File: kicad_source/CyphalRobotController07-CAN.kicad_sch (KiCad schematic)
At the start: 20 parts, among them J1 BM04B-SRSS-TB, J15 PinHeader_1x04, J16 PinHeader_1x04, J17 PinHeader_1x05, J2 RASPBERRYPI_PICO, J3 BM04B-SRSS-TB, J4 B3B-PH-SM4-TB, SW1 PTS636 SM43 SMTR LFS, U1 24LC64-I/SN

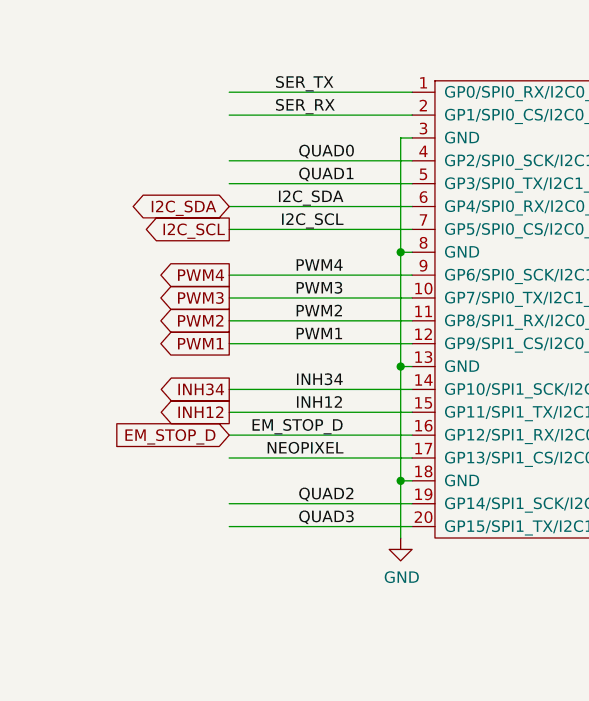
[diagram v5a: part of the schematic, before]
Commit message: added JST XH connector for motor and encoder
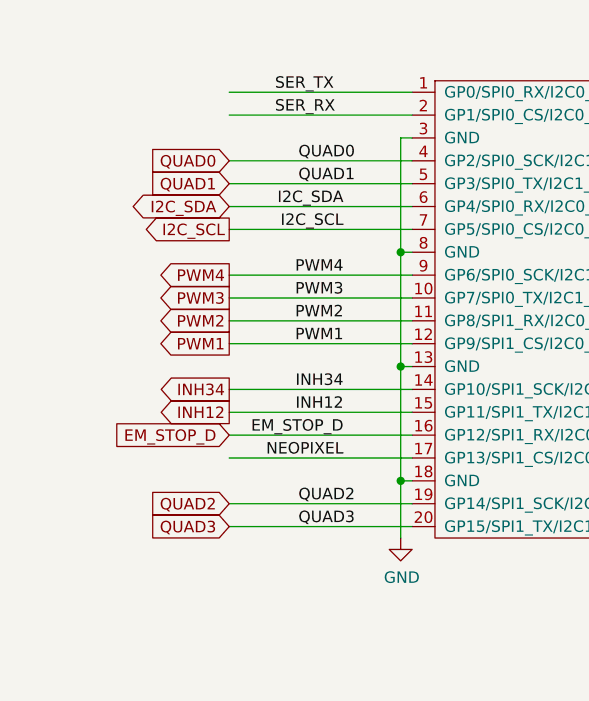
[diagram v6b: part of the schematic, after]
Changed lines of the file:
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@@
+    )
+  )
+  (global_label "QUAD1" (shape input) (at 40.64 41.91 180) (fields_autoplaced)
+    (effects (font (size 1.27 1.27)) (justify right))
+    (property "Referenzen zwischen Schaltplänen" "${INTERSHEET_REFS}" (id 0) (at 32.0868 41.8306 0)
+      (effects (font (size 1.27 1.27)) (justify right) hide)
     )
   )
@@
     )
   )
+  (global_label "QUAD2" (shape input) (at 40.64 77.47 180) (fields_autoplaced)
+    (effects (font (size 1.27 1.27)) (justify right))
+    (property "Referenzen zwischen Schaltplänen" "${INTERSHEET_REFS}" (id 0) (at 32.0868 77.3906 0)
+      (effects (font (size 1.27 1.27)) (justify right) hide)
+    )
+  )
   (global_label "PWM3" (shape output) (at 40.64 54.61 180) (fields_autoplaced)
     (effects (font (size 1.27 1.27)) (justify right))
@@
     )
   )
+  (global_label "QUAD3" (shape input) (at 40.64 80.01 180) (fields_autoplaced)
+    (effects (font (size 1.27 1.27)) (justify right))
+    (property "Referenzen zwischen Schaltplänen" "${INTERSHEET_REFS}" (id 0) (at 32.0868 79.9306 0)
+      (effects (font (size 1.27 1.27)) (justify right) hide)
+    )
+  )
   (global_label "OUTPUT0" (shape output) (at 161.29 64.77 0) (fields_autoplaced)
     (effects (font (size 1.27 1.27)) (justify left))
@@
     (property "Referenzen zwischen Schaltplänen" "${INTERSHEET_REFS}" (id 0) (at -72.39 -7.62 0)
       (effects (font (size 1.27 1.27)) hide)
+    )
+  )
+  (global_label "QUAD0" (shape input) (at 40.64 39.37 180) (fields_autoplaced)
+    (effects (font (size 1.27 1.27)) (justify right))
+    (property "Referenzen zwischen Schaltplänen" "${INTERSHEET_REFS}" (id 0) (at 32.0868 39.2906 0)
+      (effects (font (size 1.27 1.27)) (justify right) hide)
     )
   )
@@
       (reference "#PWR043") (unit 1) (value "GND") (footprint "")
     )
+    (path "/29c3546c-5738-4410-83a1-968e85712add/5bfbf133-5ed7-46d0-b93e-5a5eeb84dcff"
+      (reference "#PWR044") (unit 1) (value "+3.3V") (footprint "")
+    )
+    (path "/29c3546c-5738-4410-83a1-968e85712add/09e143e1-e556-491f-aa8e-93db6198adbc"
+      (reference "#PWR045") (unit 1) (value "GND") (footprint "")
+    )
     (path "/29c3546c-5738-4410-83a1-968e85712add/00000000-0000-0000-0000-00005df76577"
       (reference "#PWR046") (unit 1) (value "GND") (footprint "")
@@
       (reference "#PWR047") (unit 1) (value "GND") (footprint "")
     )
+    (path "/29c3546c-5738-4410-83a1-968e85712add/900bbe2d-04d2-4af8-9360-ab393613f74d"
+      (reference "#PWR048") (unit 1) (value "+3.3V") (footprint "")
+    )
     (path "/29c3546c-5738-4410-83a1-968e85712add/00000000-0000-0000-0000-00005df4db84"
       (reference "#PWR049") (unit 1) (value "GND") (footprint "")
@@
       (reference "#PWR069") (unit 1) (value "GND") (footprint "")
     )
+    (path "/29c3546c-5738-4410-83a1-968e85712add/99d4c74d-1d3b-4c55-ad7e-4e7a828dae09"
+      (reference "#PWR070") (unit 1) (value "GND") (footprint "")
+    )
     (path "/f22e738d-7eb9-478a-98ea-a8bc262180f6/00000000-0000-0000-0000-00005de82a78"
       (reference "#PWR071") (unit 1) (value "GND") (footprint "")
@@
       (reference "J18") (unit 1) (value "Conn_01x02") (footprint "Connector_Phoenix_MC:PhoenixContact_MC_1,5_2-G-3.81_1x02_P3.81mm_Horizontal")
     )
+    (path "/29c3546c-5738-4410-83a1-968e85712add/c27c1f18-6b03-4d6c-bd65-28137af7a5e4"
+      (reference "J19") (unit 1) (value "S6B-XH-A") (footprint "Connector_JST:JST_XH_S6B-XH-A_1x06_P2.50mm_Horizontal")
+    )
+    (path "/29c3546c-5738-4410-83a1-968e85712add/9ba7b6bd-56ab-4aef-8340-78cdea895920"
+      (reference "J20") (unit 1) (value "S6B-XH-A") (footprint "Connector_JST:JST_XH_S6B-XH-A_1x06_P2.50mm_Horizontal")
+    )
     (path "/00000000-0000-0000-0000-0000625bb6fe"

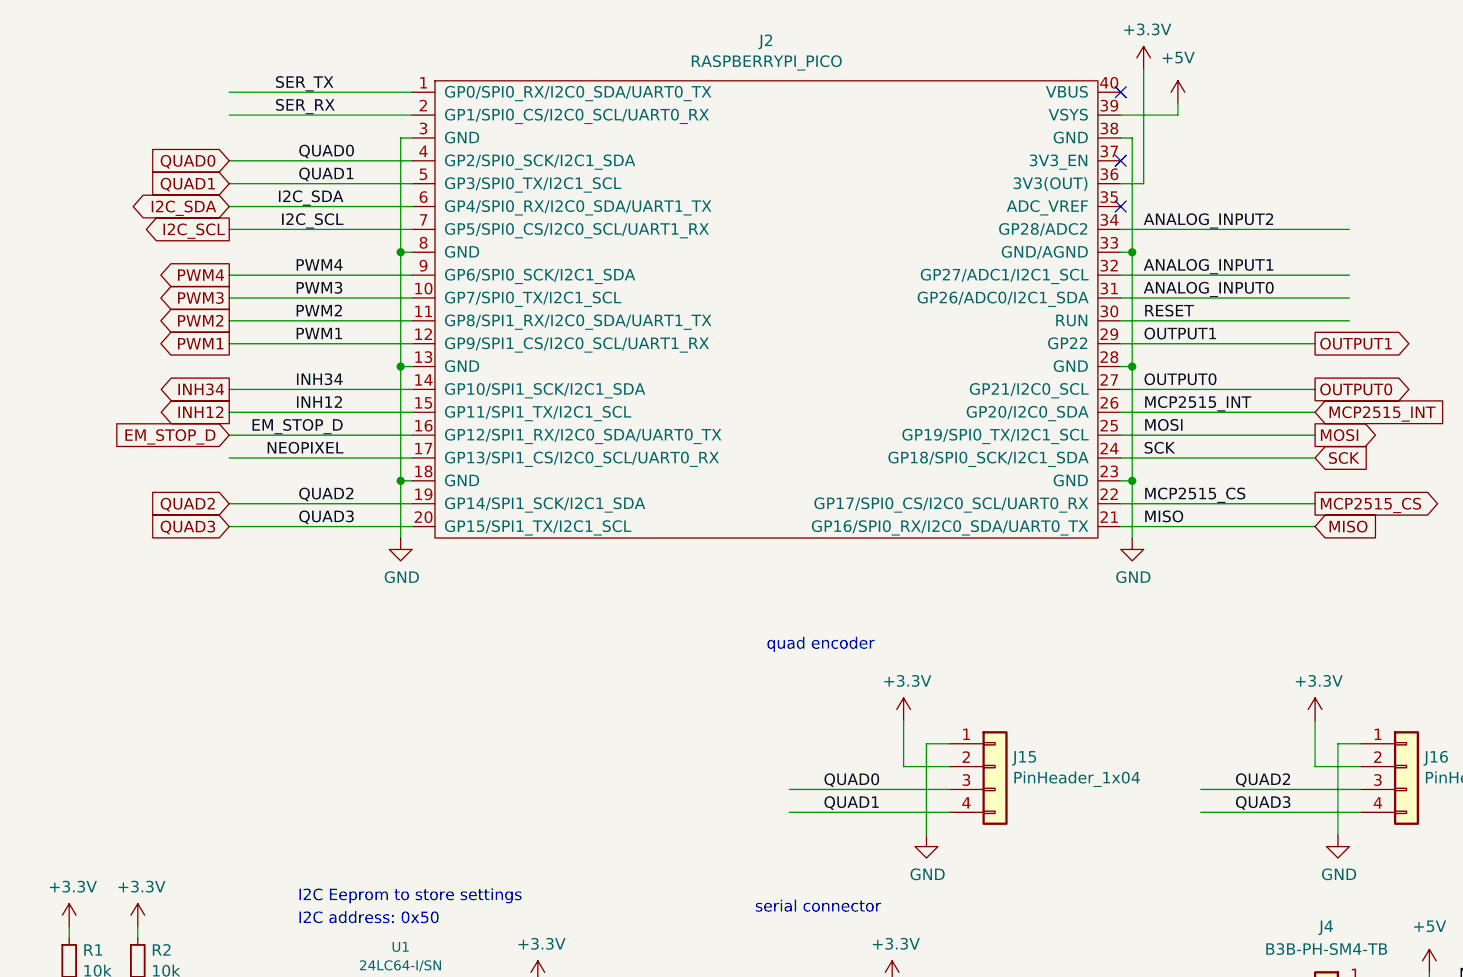
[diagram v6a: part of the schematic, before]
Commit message: changed motor connector, connected encoder
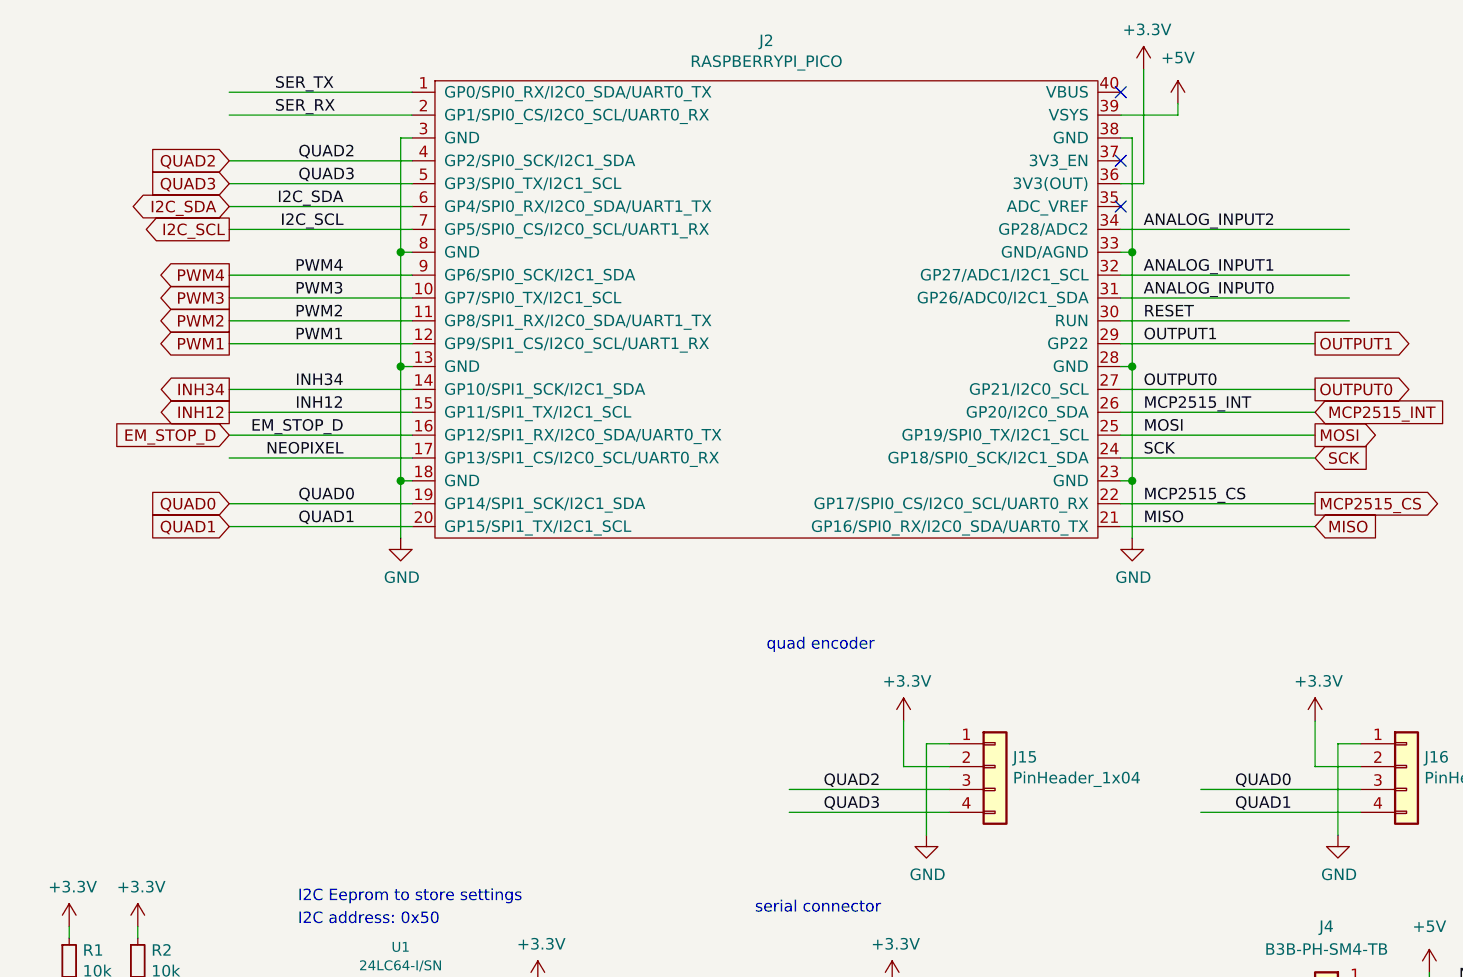
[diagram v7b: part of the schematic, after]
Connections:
- net QUAD0: now also J16.3 (Pin_3), J2.19 (GP14/SPI1_SCK/I2C1_SDA); no longer J15.3 (Pin_3), J2.4 (GP2/SPI0_SCK/I2C1_SDA)
- net QUAD1: now also J16.4 (Pin_4), J2.20 (GP15/SPI1_TX/I2C1_SCL); no longer J15.4 (Pin_4), J2.5 (GP3/SPI0_TX/I2C1_SCL)
- net QUAD2: now also J15.3 (Pin_3), J2.4 (GP2/SPI0_SCK/I2C1_SDA); no longer J16.3 (Pin_3), J2.19 (GP14/SPI1_SCK/I2C1_SDA)
- net QUAD3: now also J15.4 (Pin_4), J2.5 (GP3/SPI0_TX/I2C1_SCL); no longer J16.4 (Pin_4), J2.20 (GP15/SPI1_TX/I2C1_SCL)
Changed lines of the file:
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@@
   (title_block
     (title "CyphalRobotController07/CAN")
-    (date "2023-12-03")
+    (date "2024-01-04")
     (rev "0.2")
     (company "generationmake")
@@
     (effects (font (size 1.27 1.27)) (justify left bottom))
   )
-  (label "QUAD1" (at 106.68 111.76 0)
+  (label "QUAD3" (at 106.68 111.76 0)
     (effects (font (size 1.27 1.27)) (justify left bottom))
   )
@@
     (effects (font (size 1.27 1.27)) (justify left bottom))
   )
-  (label "QUAD0" (at 106.68 109.22 0)
+  (label "QUAD2" (at 106.68 109.22 0)
     (effects (font (size 1.27 1.27)) (justify left bottom))
   )
@@
     (effects (font (size 1.27 1.27)) (justify right bottom))
   )
-  (label "QUAD2" (at 152.4 109.22 0)
-    (effects (font (size 1.27 1.27)) (justify left bottom))
-  )
-  (label "QUAD1" (at 54.61 41.91 180)
+  (label "QUAD0" (at 152.4 109.22 0)
+    (effects (font (size 1.27 1.27)) (justify left bottom))
+  )
+  (label "QUAD3" (at 54.61 41.91 180)
     (effects (font (size 1.27 1.27)) (justify right bottom))
   )
@@
     (effects (font (size 1.27 1.27)) (justify right bottom))
   )
-  (label "QUAD3" (at 152.4 111.76 0)
+  (label "QUAD1" (at 152.4 111.76 0)
     (effects (font (size 1.27 1.27)) (justify left bottom))
   )
@@
     (effects (font (size 1.27 1.27)) (justify right bottom))
   )
-  (label "QUAD2" (at 54.61 77.47 180)
+  (label "QUAD0" (at 54.61 77.47 180)
     (effects (font (size 1.27 1.27)) (justify right bottom))
   )
@@
     (effects (font (size 1.27 1.27)) (justify left bottom))
   )
-  (label "QUAD0" (at 54.61 39.37 180)
+  (label "QUAD2" (at 54.61 39.37 180)
     (effects (font (size 1.27 1.27)) (justify right bottom))
   )
@@
     (effects (font (size 1.27 1.27)) (justify left bottom))
   )
-  (label "QUAD3" (at 54.61 80.01 180)
+  (label "QUAD1" (at 54.61 80.01 180)
     (effects (font (size 1.27 1.27)) (justify right bottom))
   )
@@
     )
   )
-  (global_label "QUAD1" (shape input) (at 40.64 41.91 180) (fields_autoplaced)
+  (global_label "QUAD3" (shape input) (at 40.64 41.91 180) (fields_autoplaced)
     (effects (font (size 1.27 1.27)) (justify right))
     (property "Referenzen zwischen Schaltplänen" "${INTERSHEET_REFS}" (id 0) (at 32.0868 41.8306 0)
@@
     )
   )
-  (global_label "QUAD2" (shape input) (at 40.64 77.47 180) (fields_autoplaced)
+  (global_label "QUAD0" (shape input) (at 40.64 77.47 180) (fields_autoplaced)
     (effects (font (size 1.27 1.27)) (justify right))
     (property "Referenzen zwischen Schaltplänen" "${INTERSHEET_REFS}" (id 0) (at 32.0868 77.3906 0)
@@
     )
   )
-  (global_label "QUAD3" (shape input) (at 40.64 80.01 180) (fields_autoplaced)
+  (global_label "QUAD1" (shape input) (at 40.64 80.01 180) (fields_autoplaced)
     (effects (font (size 1.27 1.27)) (justify right))
     (property "Referenzen zwischen Schaltplänen" "${INTERSHEET_REFS}" (id 0) (at 32.0868 79.9306 0)
@@
     )
   )
-  (global_label "QUAD0" (shape input) (at 40.64 39.37 180) (fields_autoplaced)
+  (global_label "QUAD2" (shape input) (at 40.64 39.37 180) (fields_autoplaced)
     (effects (font (size 1.27 1.27)) (justify right))
     (property "Referenzen zwischen Schaltplänen" "${INTERSHEET_REFS}" (id 0) (at 32.0868 39.2906 0)
@@
     )
     (path "/29c3546c-5738-4410-83a1-968e85712add/00000000-0000-0000-0000-00005ddbb53a"
-      (reference "J8") (unit 1) (value "x") (footprint "Connector_Phoenix_MC:PhoenixContact_MC_1,5_2-G-3.81_1x02_P3.81mm_Horizontal")
+      (reference "J8") (unit 1) (value "x") (footprint "Connector_Phoenix_MSTB:PhoenixContact_MSTBA_2,5_2-G-5,08_1x02_P5.08mm_Horizontal")
     )
     (path "/29c3546c-5738-4410-83a1-968e85712add/00000000-0000-0000-0000-00005ddbbd18"
-      (reference "J9") (unit 1) (value "x") (footprint "Connector_Phoenix_MC:PhoenixContact_MC_1,5_2-G-3.81_1x02_P3.81mm_Horizontal")
+      (reference "J9") (unit 1) (value "x") (footprint "Connector_Phoenix_MSTB:PhoenixContact_MSTBA_2,5_2-G-5,08_1x02_P5.08mm_Horizontal")
     )
     (path "/f6991e94-53cb-4fca-aa37-9cb14fb10fcb/0da4a75b-e379-4eb7-9641-dfa55c432ef5"
